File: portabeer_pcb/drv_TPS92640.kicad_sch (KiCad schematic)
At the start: 23 parts, among them Q12 Si7336ADP, Q16 Si7336ADP, U14 TPS92640PWP/NOPB

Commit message: electronics diagram and schematic
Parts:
- C66: footprint (none) -> Capacitor_THT:CP_Radial_D10.0mm_P5.00mm
- D15: footprint Diode_SMD:D_SOD-523 -> Diode_SMD:D_SOD-123
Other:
- company: (none) -> ©2024 Luca Anastasio
- title: (none) -> Beerpak
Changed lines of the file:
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@@
 	(generator_version "8.0")
 	(paper "A4")
+	(title_block
+		(title "Beerpak")
+		(company "©2024 Luca Anastasio")
+	)
 	(junction
 		(at 241.3 78.74)
@@
 			)
 		)
-		(property "Footprint" ""
+		(property "Footprint" "Capacitor_THT:CP_Radial_D10.0mm_P5.00mm"
 			(at 70.8152 35.56 0)
 			(effects
@@
 			)
 		)
-		(property "Footprint" "Diode_SMD:D_SOD-523"
+		(property "Footprint" "Diode_SMD:D_SOD-123"
 			(at 145.415 60.96 0)
 			(effects

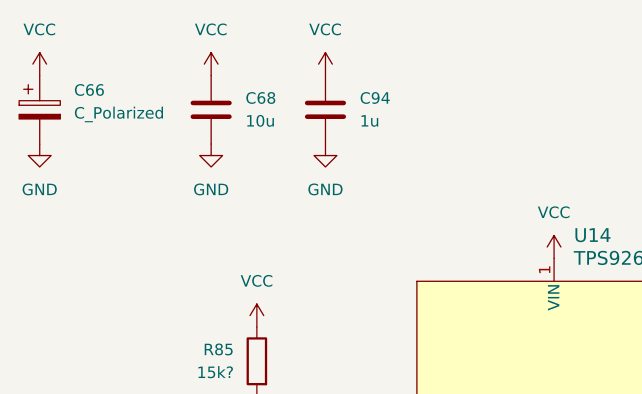
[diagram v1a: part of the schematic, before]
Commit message: added 3d models, started layout
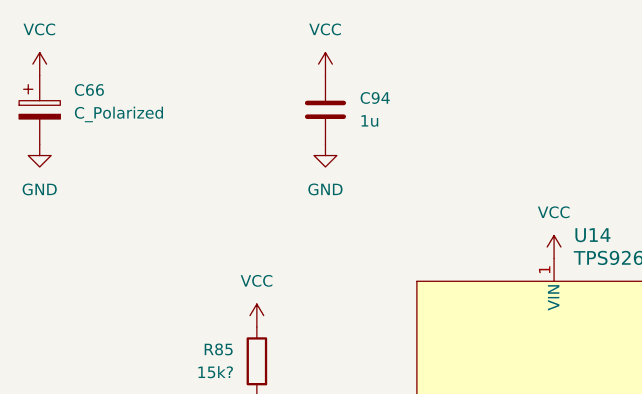
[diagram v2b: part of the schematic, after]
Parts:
- removed C68: 10u, Capacitor_SMD:C_1206_3216Metric, symbol Device:C
- C66: footprint Capacitor_THT:CP_Radial_D10.0mm_P5.00mm -> Capacitor_THT:CP_Radial_D8.0mm_P3.50mm
- Q12, Q16: footprint Package_SO:PowerPAK_SO-8_Single -> portabeer:PowerPAK_SO-8_Single
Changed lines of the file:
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@@
 			)
 		)
-		(property "Footprint" "Package_SO:PowerPAK_SO-8_Single"
+		(property "Footprint" "portabeer:PowerPAK_SO-8_Single"
 			(at 193.04 88.265 0)
 			(effects
@@
 			)
 		)
-		(property "Footprint" "Capacitor_THT:CP_Radial_D10.0mm_P5.00mm"
+		(property "Footprint" "Capacitor_THT:CP_Radial_D8.0mm_P3.50mm"
 			(at 70.8152 35.56 0)
 			(effects
@@
 	)
 	(symbol
-		(lib_id "power:VCC")
-		(at 88.9 27.94 0)
-		(unit 1)
-		(exclude_from_sim no)
-		(in_bom yes)
-		(on_board yes)
-		(dnp no)
-		(fields_autoplaced yes)
-		(property "Reference" "#PWR0217"
-			(at 88.9 31.75 0)
-			(effects
-				(font
-					(size 1.27 1.27)
-				)
-				(hide yes)
-			)
-		)
-		(property "Value" "VCC"
-			(at 88.9 22.86 0)
-			(effects
-				(font
-					(size 1.27 1.27)
-				)
-			)
-		)
-		(property "Footprint" ""
-			(at 88.9 27.94 0)
-			(effects
-				(font
-					(size 1.27 1.27)
-				)
-				(hide yes)
-			)
-		)
-		(property "Datasheet" ""
-			(at 88.9 27.94 0)
-			(effects
-				(font
-					(size 1.27 1.27)
-				)
-				(hide yes)
-			)
-		)
-		(property "Description" "Power symbol creates a global label with name \"VCC\""
-			(at 88.9 27.94 0)
-			(effects
-				(font
-					(size 1.27 1.27)
-				)
-				(hide yes)
-			)
-		)
-		(pin "1"
-		)
-		(instances
-			(project "portabeer_pcb"
-				(path "/bb676e84-aa44-417a-9a70-748af1c322fb/420d7ab6-7a6e-404c-b820-acde96549ae5/d5db841d-87ae-4782-b433-7e903d5a1efe"
-					(reference "#PWR0217")
-					(unit 1)
-				)
-				(path "/bb676e84-aa44-417a-9a70-748af1c322fb/82d26029-2514-464b-b918-c848fe41d8d3/d5db841d-87ae-4782-b433-7e903d5a1efe"
-					(reference "#PWR0262")
-					(unit 1)
-				)
-			)
-		)
-	)
-	(symbol
 		(lib_id "power:GND")
 		(at 215.9 101.6 0)
@@
 	)
 	(symbol
-		(lib_id "power:GND")
-		(at 88.9 35.56 0)
-		(unit 1)
-		(exclude_from_sim no)
-		(in_bom yes)
-		(on_board yes)
-		(dnp no)
-		(fields_autoplaced yes)
-		(property "Reference" "#PWR0218"
-			(at 88.9 41.91 0)
-			(effects
-				(font
-					(size 1.27 1.27)
-				)
-				(hide yes)
-			)
-		)
-		(property "Value" "GND"
-			(at 88.9 40.64 0)
-			(effects
-				(font
-					(size 1.27 1.27)
-				)
-			)
-		)
-		(property "Footprint" ""
-			(at 88.9 35.56 0)
-			(effects
-				(font
-					(size 1.27 1.27)
-				)
-				(hide yes)
-			)
-		)
-		(property "Datasheet" ""
-			(at 88.9 35.56 0)
-			(effects
-				(font
-					(size 1.27 1.27)
-				)
-				(hide yes)
-			)
-		)
-		(property "Description" "Power symbol creates a global label with name \"GND\" , ground"
-			(at 88.9 35.56 0)
-			(effects
-				(font
-					(size 1.27 1.27)
-				)
-				(hide yes)
-			)
-		)
-		(pin "1"
-		)
-		(instances
-			(project "portabeer_pcb"
-				(path "/bb676e84-aa44-417a-9a70-748af1c322fb/420d7ab6-7a6e-404c-b820-acde96549ae5/d5db841d-87ae-4782-b433-7e903d5a1efe"
-					(reference "#PWR0218")
-					(unit 1)
-				)
-				(path "/bb676e84-aa44-417a-9a70-748af1c322fb/82d26029-2514-464b-b918-c848fe41d8d3/d5db841d-87ae-4782-b433-7e903d5a1efe"
-					(reference "#PWR0263")
-					(unit 1)
-				)
-			)
-		)
-	)
-	(symbol
 		(lib_id "Transistor_FET:Si7336ADP")
 		(at 187.96 71.12 0)
@@
 			)
 		)
-		(property "Footprint" "Package_SO:PowerPAK_SO-8_Single"
+		(property "Footprint" "portabeer:PowerPAK_SO-8_Single"
 			(at 193.04 73.025 0)
 			(effects
@@
 					(unit 1)
 				)
-			)
-		)
-	)
-	(symbol
-		(lib_id "Device:C")
-		(at 88.9 31.75 0)
-		(unit 1)
-		(exclude_from_sim no)
-		(in_bom yes)
-		(on_board yes)
-		(dnp no)
-		(fields_autoplaced yes)
-		(property "Reference" "C68"
-			(at 92.71 30.4799 0)
-			(effects
-				(font
-					(size 1.27 1.27)
-				)
-				(justify left)
-			)
-		)
-		(property "Value" "10u"
-			(at 92.71 33.0199 0)
-			(effects
-				(font
-					(size 1.27 1.27)
-				)
-				(justify left)
-			)
-		)
-		(property "Footprint" "Capacitor_SMD:C_1206_3216Metric"
-			(at 89.8652 35.56 0)
-			(effects
-				(font
-					(size 1.27 1.27)
-				)
-				(hide yes)
-			)
-		)
-		(property "Datasheet" "~"
-			(at 88.9 31.75 0)
-			(effects
-				(font
-					(size 1.27 1.27)
-				)
-				(hide yes)
-			)
-		)
-		(property "Description" "Unpolarized capacitor"
-			(at 88.9 31.75 0)
-			(effects
-				(font
-					(size 1.27 1.27)
-				)
-				(hide yes)
-			)
-		)
-		(pin "2"
-		)
-		(pin "1"
-		)
-		(instances
-			(project "portabeer_pcb"
-				(path "/bb676e84-aa44-417a-9a70-748af1c322fb/420d7ab6-7a6e-404c-b820-acde96549ae5/d5db841d-87ae-4782-b433-7e903d5a1efe"
-					(reference "C68")
-					(unit 1)
-				)
-				(path "/bb676e84-aa44-417a-9a70-748af1c322fb/82d26029-2514-464b-b918-c848fe41d8d3/d5db841d-87ae-4782-b433-7e903d5a1efe"
-					(reference "C81")
-					(unit 1)
-				)

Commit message: layout
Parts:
- added HS1: Heatsink, portabeer:Heatsink_14x14x6mm_adhesive, symbol Mechanical:Heatsink
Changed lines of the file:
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@@
+	)
+	(symbol
+		(lib_id "Mechanical:Heatsink")
+		(at 190.5 53.34 0)
+		(unit 1)
+		(exclude_from_sim yes)
+		(in_bom yes)
+		(on_board yes)
+		(dnp no)
+		(fields_autoplaced yes)
+		(property "Reference" "HS1"
+			(at 194.31 50.1649 0)
+			(effects
+				(font
+					(size 1.27 1.27)
+				)
+				(justify left)
+			)
+		)
+		(property "Value" "Heatsink"
+			(at 194.31 52.7049 0)
+			(effects
+				(font
+					(size 1.27 1.27)
+				)
+				(justify left)
+			)
+		)
+		(property "Footprint" "portabeer:Heatsink_14x14x6mm_adhesive"
+			(at 190.8048 53.34 0)
+			(effects
+				(font
+					(size 1.27 1.27)
+				)
+				(hide yes)
+			)
+		)
+		(property "Datasheet" "~"
+			(at 190.8048 53.34 0)
+			(effects
+				(font
+					(size 1.27 1.27)
+				)
+				(hide yes)
+			)
+		)
+		(property "Description" "Heatsink"
+			(at 190.5 53.34 0)
+			(effects
+				(font
+					(size 1.27 1.27)
+				)
+				(hide yes)
+			)
+		)
+		(instances
+			(project ""
+				(path "/bb676e84-aa44-417a-9a70-748af1c322fb/420d7ab6-7a6e-404c-b820-acde96549ae5/d5db841d-87ae-4782-b433-7e903d5a1efe"
+					(reference "HS1")
+					(unit 1)
+				)
+				(path "/bb676e84-aa44-417a-9a70-748af1c322fb/82d26029-2514-464b-b918-c848fe41d8d3/d5db841d-87ae-4782-b433-7e903d5a1efe"
+					(reference "HS2")
+					(unit 1)
+				)
+			)
+		)
 	)
 	(symbol
